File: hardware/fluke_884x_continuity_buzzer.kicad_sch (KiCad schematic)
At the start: 64 parts, among them J2 Conn_01x02, J203 16 pin DIP socket, J204 16 pin DIP socket, J3 USB_B_Micro, P203 16 pin DIP plug, P204 16 pin DIP plug, U1 AZ117EH-3.3, U2 W25Q128JVS, U3 RP2040, U4 umw_78l05_sot23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

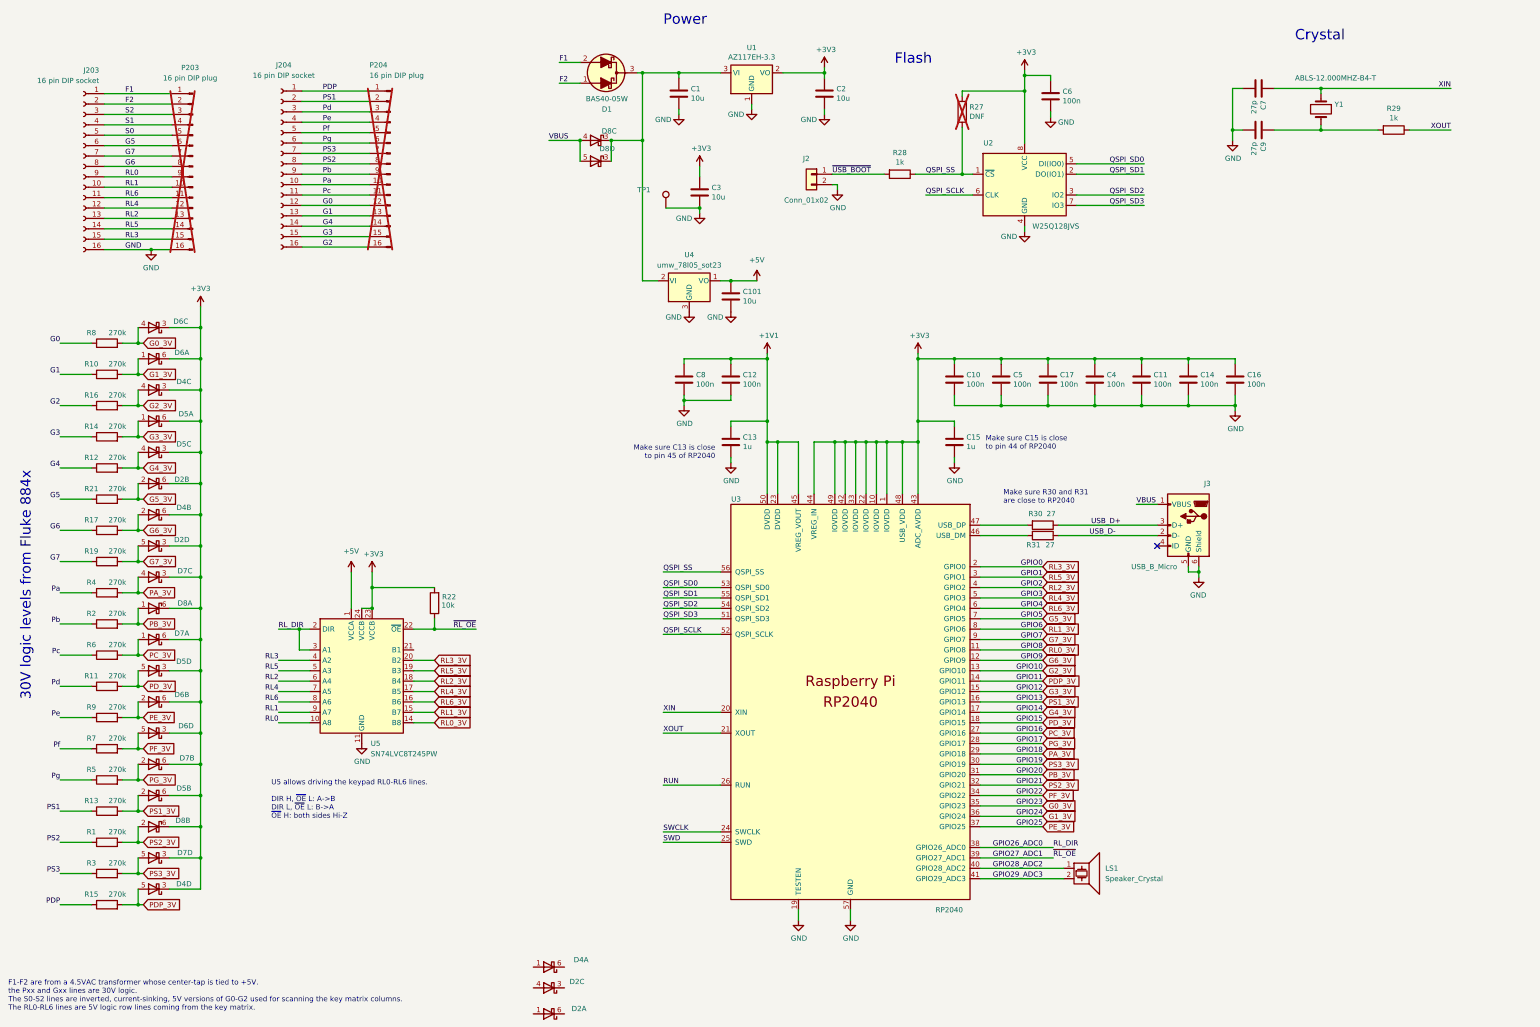
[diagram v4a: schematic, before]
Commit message: Change R1-R19 to 200k
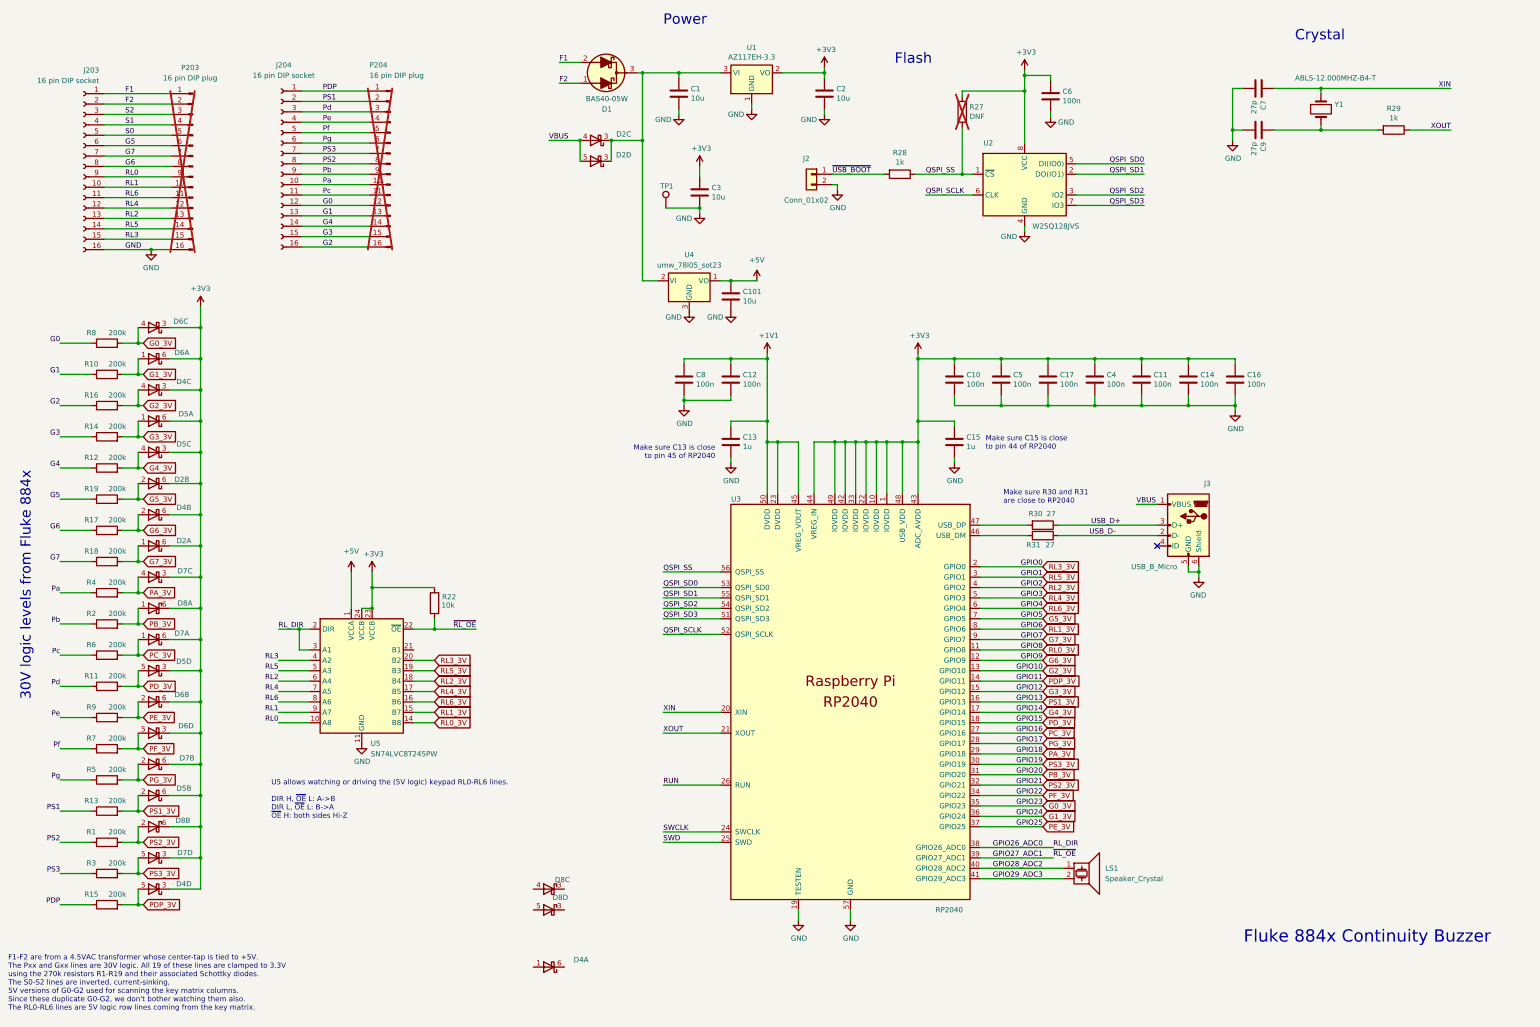
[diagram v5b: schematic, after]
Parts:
- R1, R10, R11, R12, R13, R14, R15, R16, R17, R2, R3, R4, R5, R6, R7, R8, R9: value 270k -> 200k; LCSC C25550 -> C25764
- R18: renamed from R19; value 270k -> 200k; LCSC C25550 -> C25764
- R19: renamed from R21; value 270k -> 200k; LCSC C25550 -> C25764
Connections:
- net +3V3: now also D2.6 (K); no longer D2.3 (K)
- net G7_3V: now also D2.1 (A); no longer D2.5 (A)
- net VBUS: now also D2.4 (A), D2.5 (A); no longer D8.4 (A), D8.5 (A)
- net at C1.1, D1.3 (K), U1.3 (VI)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: now also D2.3 (K), D2.3 (K); no longer D8.3 (K), D8.3 (K)
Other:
- note added: "F1-F2 are from a 4.5VAC transformer whose center-tap is tied to +5V. The Pxx and Gxx lines are 30V logic. All 19 of these lines are clamped to 3.3V using the 270k resistors R1-R19 and their associated Schottky diodes. The S0-S2 lines are inverted, current-sinking, 5V versions of G0-G2 used for scanning the key matrix columns. Since these duplicate G0-G2, we don't bother watching them also. The RL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"
- note added: "Fluke 884x Continuity Buzzer"
- note added: "U5 allows watching or driving the (5V logic) keypad RL0-RL6 lines. DIR H, ~{OE} L: A->B DIR L, ~{OE} L: B->A ~{OE} H: both sides Hi-Z"
- note removed: "F1-F2 are from a 4.5VAC transformer whose center-tap is tied to +5V. the Pxx and Gxx lines are 30V logic. The S0-S2 lines are inverted, current-sinking, 5V versions of G0-G2 used for scanning the key matrix columns. The RL0-RL6 lines are 5V logic row lines coming from the key matrix."
- note removed: "U5 allows driving the keypad RL0-RL6 lines. DIR H, ~{OE} L: A->B DIR L, ~{OE} L: B->A ~{OE} H: both sides Hi-Z"
- moved on the sheet: D2A, D2C, D2D, D8C, D8D

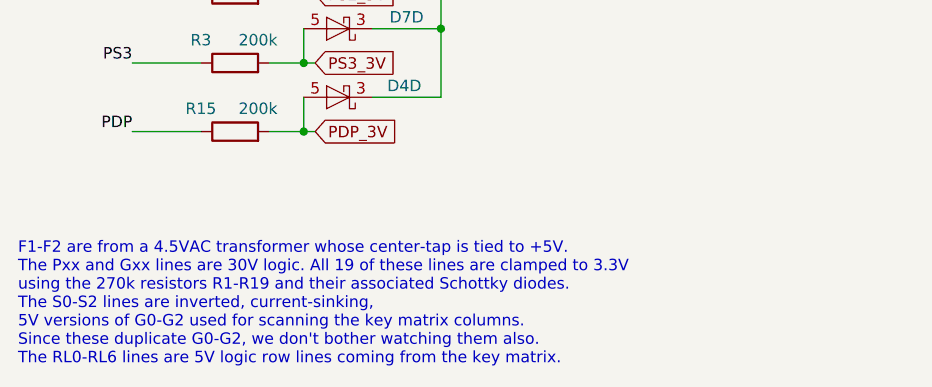
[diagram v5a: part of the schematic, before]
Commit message: Add PDF of schematic.
Also correct text in schematic.
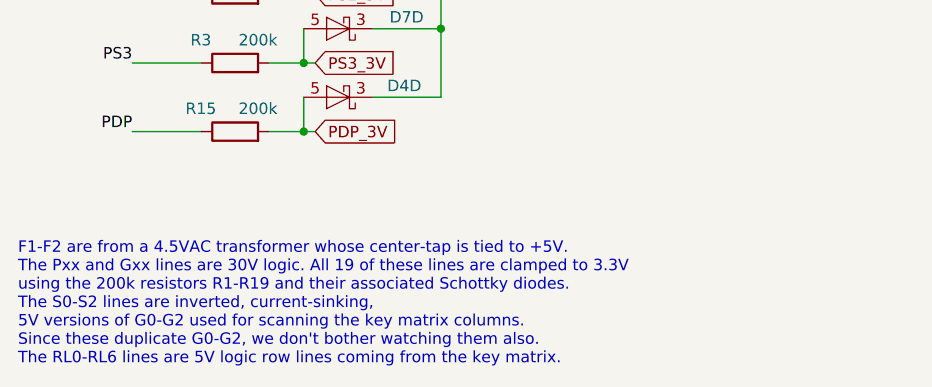
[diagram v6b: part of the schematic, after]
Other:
- note added: "F1-F2 are from a 4.5VAC transformer whose center-tap is tied to +5V. The Pxx and Gxx lines are 30V logic. All 19 of these lines are clamped to 3.3V using the 200k resistors R1-R19 and their associated Schottky diodes. The S0-S2 lines are inverted, current-sinking, 5V versions of G0-G2 used for scanning the key matrix columns. Since these duplicate G0-G2, we don't bother watching them also. The RL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"
- note removed: "F1-F2 are from a 4.5VAC transformer whose center-tap is tied to +5V. The Pxx and Gxx lines are 30V logic. All 19 of these lines are clamped to 3.3V using the 270k resistors R1-R19 and their associated Schottky diodes. The S0-S2 lines are inverted, current-sinking, 5V versions of G0-G2 used for scanning the key matrix columns. Since these duplicate G0-G2, we don't bother watching them also. The RL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"
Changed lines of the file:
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@@
 		)
 	)
-	(text "F1-F2 are from a 4.5VAC transformer whose center-tap is tied to +5V.\nThe Pxx and Gxx lines are 30V logic. All 19 of these lines are clamped to 3.3V\nusing the 270k resistors R1-R19 and their associated Schottky diodes.\nThe S0-S2 lines are inverted, current-sinking,\n5V versions of G0-G2 used for scanning the key matrix columns.\nSince these duplicate G0-G2, we don't bother watching them also.\nThe RL0-RL6 lines are 5V logic row lines coming from the key matrix."
+	(text "F1-F2 are from a 4.5VAC transformer whose center-tap is tied to +5V.\nThe Pxx and Gxx lines are 30V logic. All 19 of these lines are clamped to 3.3V\nusing the 200k resistors R1-R19 and their associated Schottky diodes.\nThe S0-S2 lines are inverted, current-sinking,\n5V versions of G0-G2 used for scanning the key matrix columns.\nSince these duplicate G0-G2, we don't bother watching them also.\nThe RL0-RL6 lines are 5V logic row lines coming from the key matrix."
 		(exclude_from_sim no)
 		(at 16.51 260.985 0)

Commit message: updating for rev3
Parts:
- removed C101: 10u, Capacitor_SMD:C_0805_2012Metric, symbol Device:C
- removed R22: 10k, Resistor_SMD:R_0402_1005Metric, symbol Device:R
- removed U4: umw_78l05_sot23, Package_TO_SOT_SMD:SOT-23-3, symbol misc:umw_78l05_sot23
- removed U5: SN74LVC8T245PW, Package_SO:TSSOP-24_4.4x7.8mm_P0.65mm, symbol Logic_LevelTranslator:SN74AVC8T245PW
- added C18: 220uF, Capacitor_THT:C_Radial_D6.3mm_H11.0mm_P2.50mm, symbol Device:C_Polarized_US
- J3: footprint Connector_USB:USB_Micro-B_Amphenol_10118194_Horizontal -> RP2040_minimal:USB_Micro-B_Amphenol_10118194_Horizontal
- TP1: footprint TestPoint:TestPoint_THTPad_D1.0mm_Drill0.5mm -> RP2040_minimal:TestPoint_Keystone_5019_Minature
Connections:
- net GND: now also C18.2
- net at C1.1, D1.3 (K), D2.3 (K)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: now also C18.1
- net RL0_3V renamed GPIO8
- net RL1_3V renamed GPIO6
- net RL2_3V renamed GPIO2
- net RL3_3V renamed GPIO0
- net RL4_3V renamed GPIO3
- net RL5_3V renamed GPIO1
- net RL6_3V renamed GPIO4
- no-connect marks 1 -> 15
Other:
- note added: "Unused"
- note removed: "U5 allows watching or driving the (5V logic) keypad RL0-RL6 lines. DIR H, ~{OE} L: A->B DIR L, ~{OE} L: B->A ~{OE} H: both sides Hi-Z"
- moved on the sheet: D1, D2C, D2D, D8C, D8D

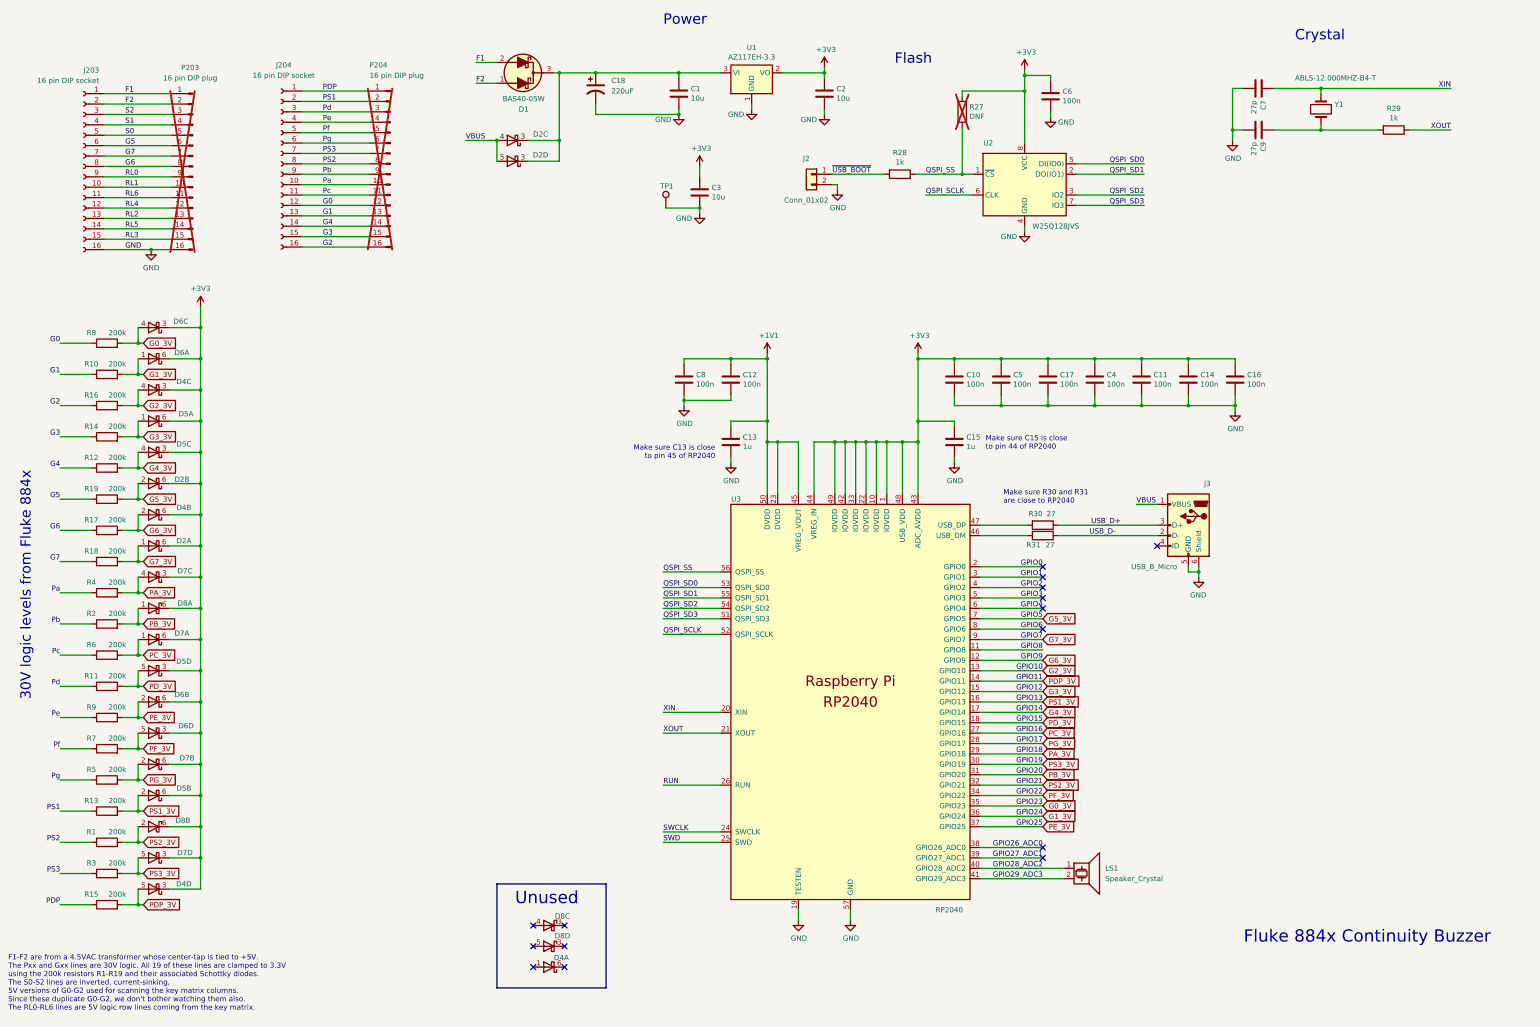
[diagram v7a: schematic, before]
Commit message: Add final parts; generate JLCPCB data
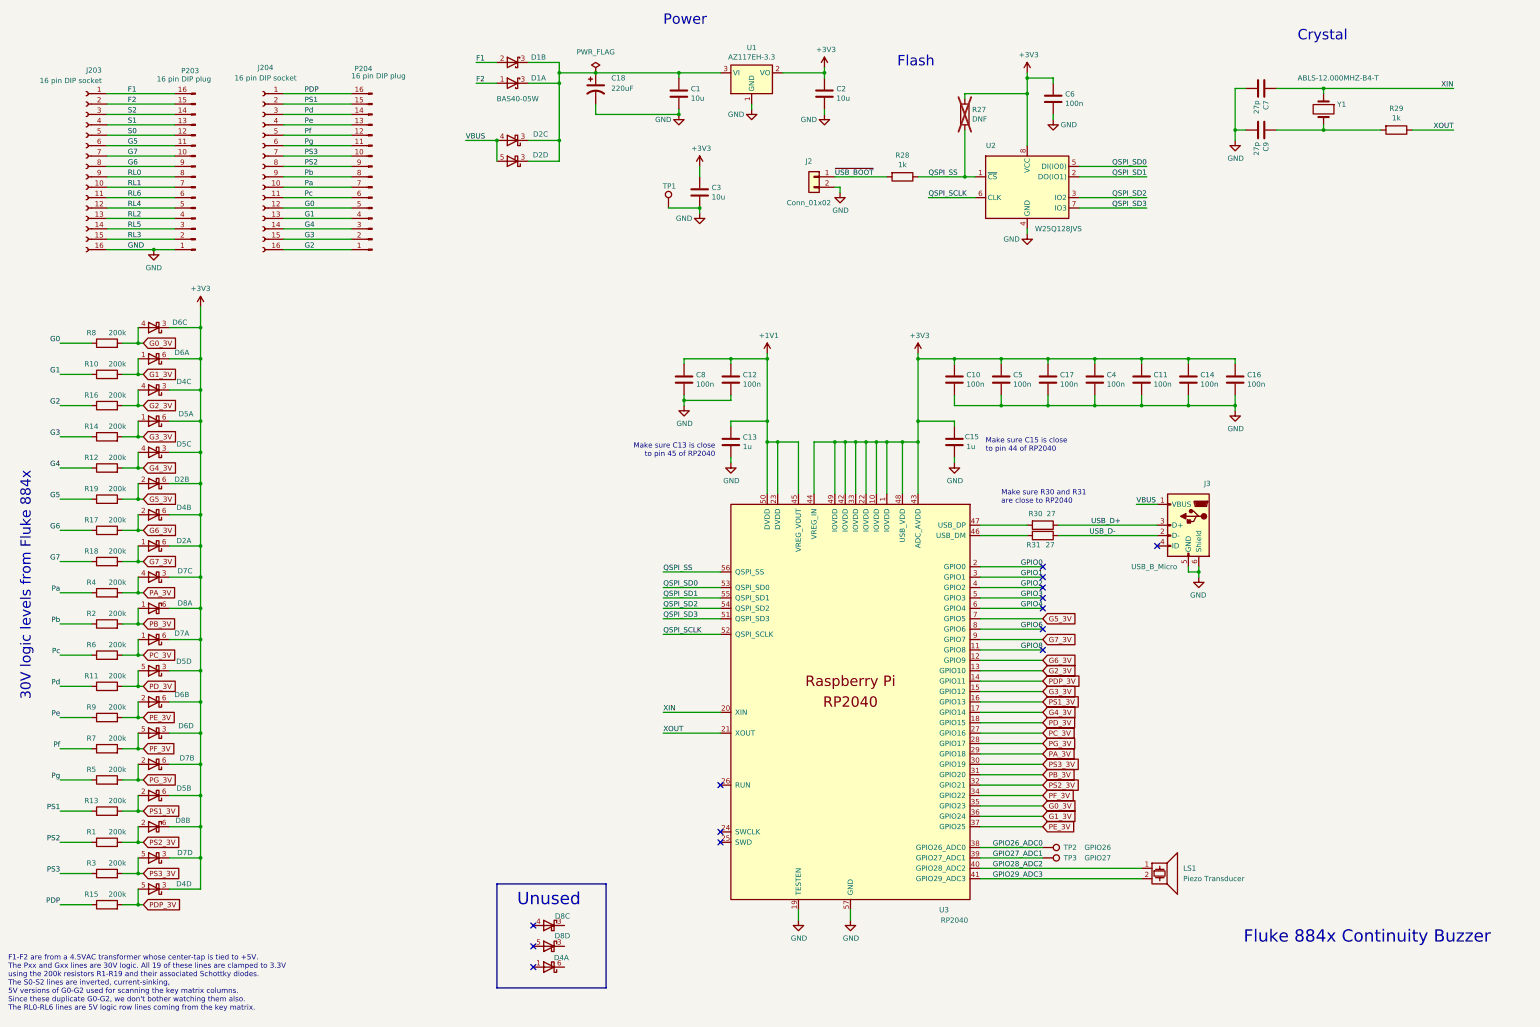
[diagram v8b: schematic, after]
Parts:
- removed D1: BAS40-05W, Package_TO_SOT_SMD:SOT-323_SC-70, symbol PCM_Diode_Schottky_AKL:BAS40-05W
- added D1: BAS40-05W, Package_TO_SOT_SMD:SOT-323_SC-70, symbol misc:bas40-05w_split
- added TP2: GPIO26, TestPoint:TestPoint_THTPad_1.0x1.0mm_Drill0.5mm, symbol Connector:TestPoint
- added TP3: GPIO27, TestPoint:TestPoint_THTPad_1.0x1.0mm_Drill0.5mm, symbol Connector:TestPoint
- C18: LCSC (none) -> C134565
- J3: symbol RP2040_minimal-rescue:USB_B_Micro-Connector -> RP2040_minimal:USB_B_Micro-Connector
- LS1: value Speaker_Crystal -> Piezo Transducer
- P203, P204: footprint Package_DIP:DIP-16_W7.62mm_Socket -> RP2040_minimal:DIP-16_W7.62mm; LCSC (none) -> C2883633; now fitted; now in the parts list
- TP1: LCSC (none) -> C238131; now in the parts list
- U2: footprint Package_SO:SOIC-8_5.23x5.23mm_P1.27mm -> RP2040_minimal:SOIC-8_5.23x5.23mm_P1.27mm; symbol RP2040_minimal-rescue:W25Q128JVS-Memory_Flash -> RP2040_minimal:W25Q128JVS-Memory_Flash
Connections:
- net F1: now also P203.16 (Pin_16), D1.2 (K); no longer P203.1 (Pin_1)
- net F2: now also P203.15 (Pin_15), D1.1 (A); no longer P203.2 (Pin_2)
- net G0: now also P204.5 (Pin_5); no longer P204.12 (Pin_12)
- net G1: now also P204.4 (Pin_4); no longer P204.13 (Pin_13)
- net G2: now also P204.1 (Pin_1); no longer P204.16 (Pin_16)
- net G3: now also P204.2 (Pin_2); no longer P204.15 (Pin_15)
- net G4: now also P204.3 (Pin_3); no longer P204.14 (Pin_14)
- net G5: now also P203.11 (Pin_11); no longer P203.6 (Pin_6)
- net G6: now also P203.9 (Pin_9); no longer P203.8 (Pin_8)
- net G7: now also P203.10 (Pin_10); no longer P203.7 (Pin_7)
- net GND: now also P203.1 (Pin_1); no longer P203.16 (Pin_16)
- net GPIO26_ADC0: now also TP2.1
- net GPIO27_ADC1: now also TP3.1
- net PDP: now also P204.16 (Pin_16); no longer P204.1 (Pin_1)
- net PS1: now also P204.15 (Pin_15); no longer P204.2 (Pin_2)
- net PS2: now also P204.9 (Pin_9); no longer P204.8 (Pin_8)
- net PS3: now also P204.10 (Pin_10); no longer P204.7 (Pin_7)
- net Pa: now also P204.7 (Pin_7); no longer P204.10 (Pin_10)
- net Pb: now also P204.8 (Pin_8); no longer P204.9 (Pin_9)
- net Pc: now also P204.6 (Pin_6); no longer P204.11 (Pin_11)
- net Pd: now also P204.14 (Pin_14); no longer P204.3 (Pin_3)
- net Pe: now also P204.13 (Pin_13); no longer P204.4 (Pin_4)
- net Pf: now also P204.12 (Pin_12); no longer P204.5 (Pin_5)
- net Pg: now also P204.11 (Pin_11); no longer P204.6 (Pin_6)
- net RL0: now also P203.8 (Pin_8); no longer P203.9 (Pin_9)
- net RL1: now also P203.7 (Pin_7); no longer P203.10 (Pin_10)
- net RL2: now also P203.4 (Pin_4); no longer P203.13 (Pin_13)
- net RL3: now also P203.2 (Pin_2); no longer P203.15 (Pin_15)
- net RL4: now also P203.5 (Pin_5); no longer P203.12 (Pin_12)
- net RL5: now also P203.3 (Pin_3); no longer P203.14 (Pin_14)
- net RL6: now also P203.6 (Pin_6); no longer P203.11 (Pin_11)
- net S0: now also P203.12 (Pin_12); no longer P203.5 (Pin_5)
- net S1: now also P203.13 (Pin_13); no longer P203.4 (Pin_4)
- net S2: now also P203.14 (Pin_14); no longer P203.3 (Pin_3)
- net at C1.1, C18.1, D2.3 (K)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: now also D1.3 (K), D1.3 (K)
- net RUN: no longer names the net of U3.26 (RUN)
- net SWCLK: no longer names the net of U3.24 (SWCLK)
- net SWD: no longer names the net of U3.25 (SWD)
- no-connect marks 15 -> 14
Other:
- moved on the sheet: C6, C7, C9, J2, J203, J204, LS1, R27, R28, R29, TP1, U2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
